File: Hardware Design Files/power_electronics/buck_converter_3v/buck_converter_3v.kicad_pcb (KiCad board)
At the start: 2 copper layers, 34.4 x 28.1 mm, 22 parts, among them J1 Conn_01x02, J2 Conn_01x02

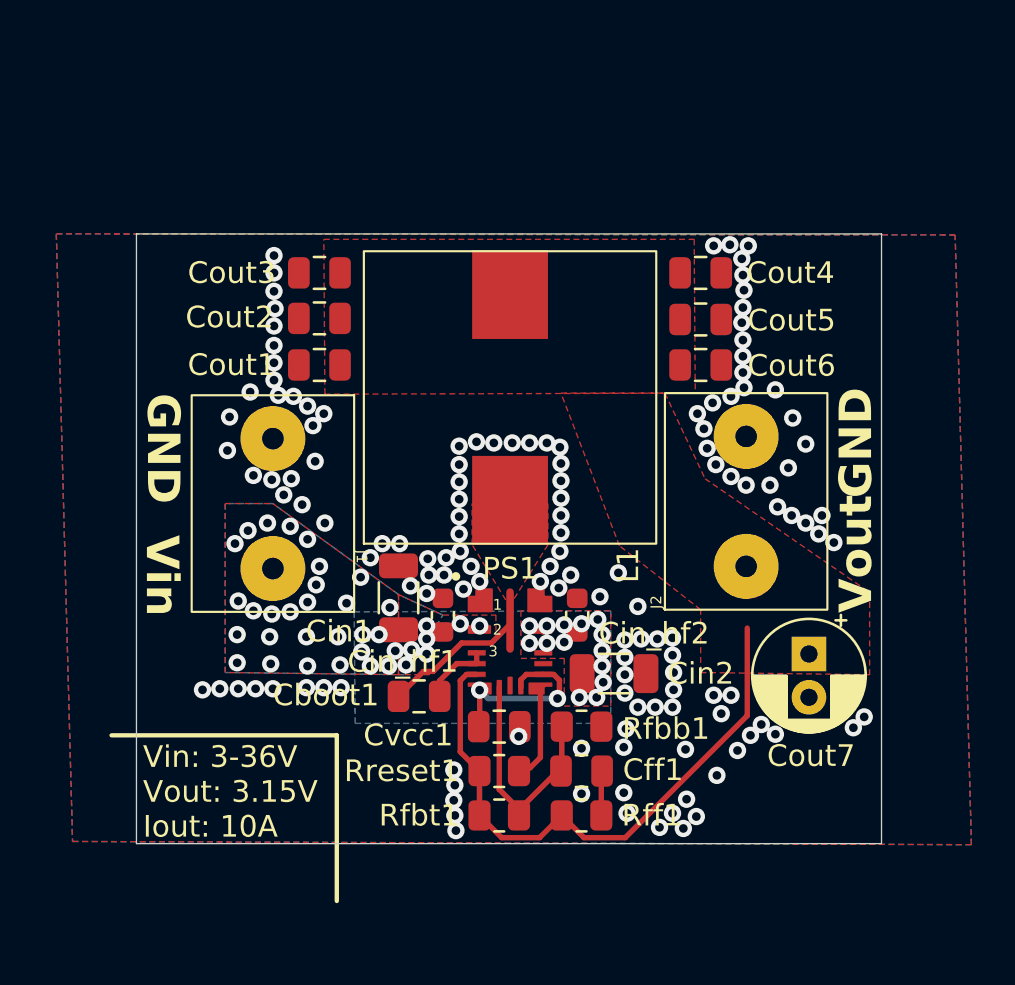
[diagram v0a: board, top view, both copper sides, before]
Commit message: refactor(buck_converter_3v): apply jlcpcb fab design rules
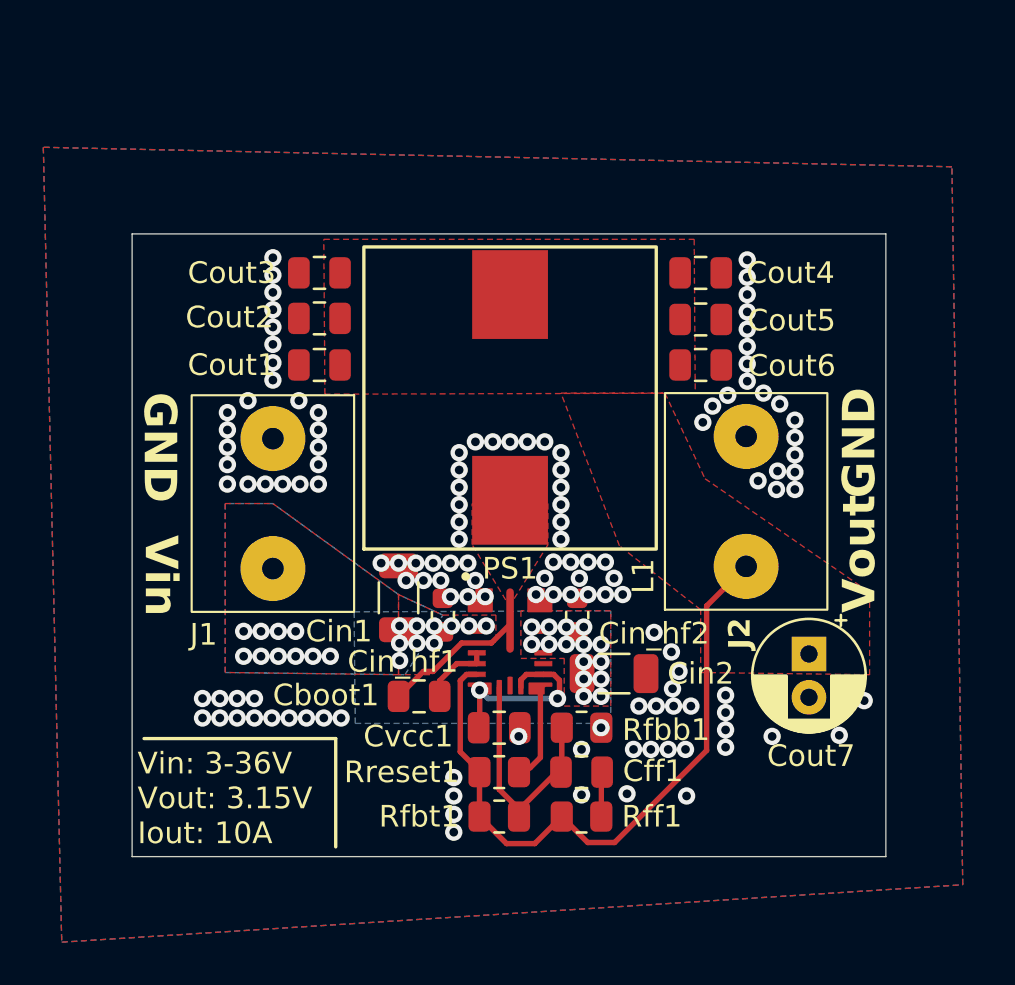
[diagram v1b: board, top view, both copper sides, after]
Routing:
- net /Vout: track 27.5 -> 30.5 mm
- net /Vin: track 0.66 -> 0.00 mm, vias 50 -> 35
- net GND: vias 141 -> 132
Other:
- board size 34.4 x 28.1 mm -> 34.8 x 28.8 mm
- rule pad_to_mask_clearance: 0.0508 -> 0.038

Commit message: feat(buck_converter): unify pcb design, schematic varies by resistor value, add mounting holes
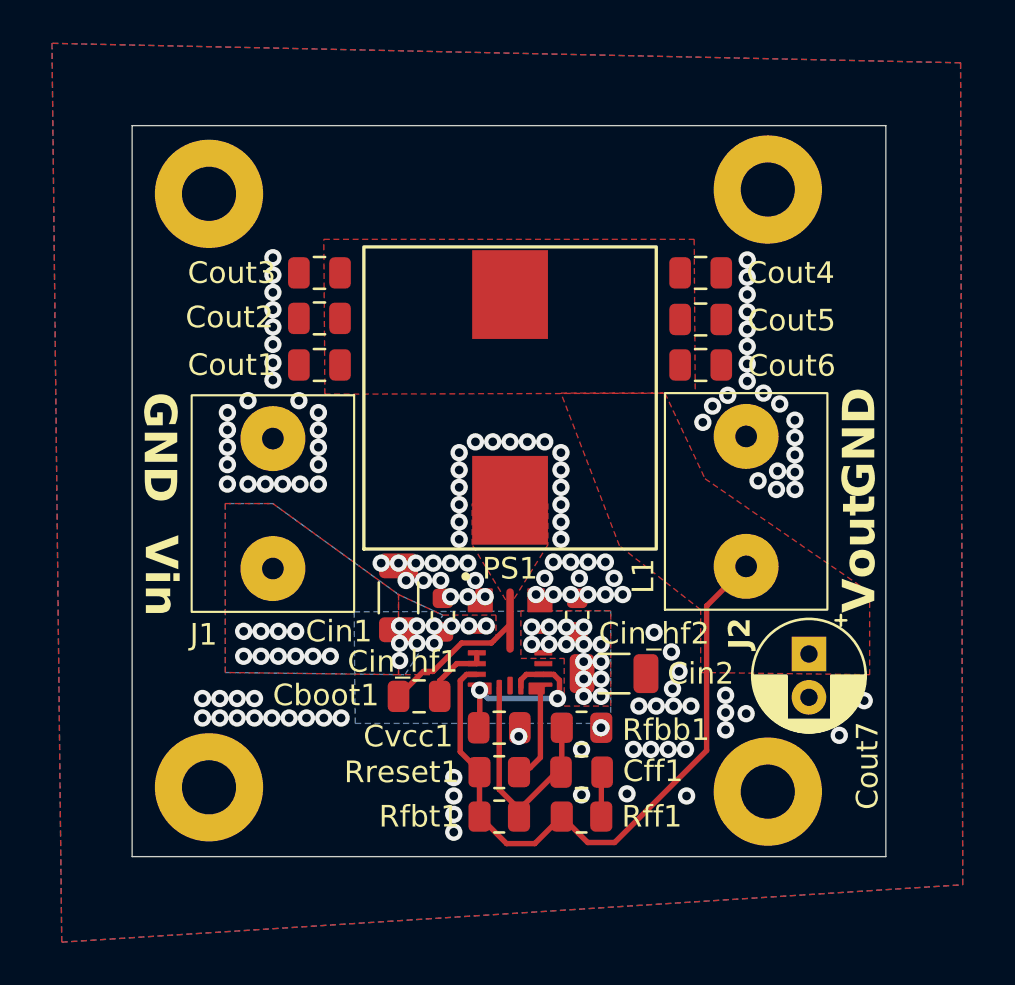
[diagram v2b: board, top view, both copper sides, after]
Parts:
- added H1: MountingHole, MountingHole:MountingHole_2.5mm_Pad, F.Cu at (95.6, 76.2)
- added H2: MountingHole, MountingHole:MountingHole_2.5mm_Pad, F.Cu at (121.4, 76.4)
- added H3: MountingHole, MountingHole:MountingHole_2.5mm_Pad, F.Cu at (121.4, 48.6)
- added H4: MountingHole, MountingHole:MountingHole_2.5mm_Pad, F.Cu at (95.6, 48.8)
- L1: value 2.2u -> 3.3u
- Rfbb1: value 46.5k -> 25.5k
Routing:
- net GND: vias 132 -> 131
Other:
- board size 34.8 x 28.8 mm -> 34.8 x 33.8 mm
- board text removed: "Vin: 3-36V Vout: 3.15V Iout: 10A"
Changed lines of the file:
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@@
     )
   )
+  (footprint "MountingHole:MountingHole_2.5mm_Pad" (layer "F.Cu")
+    (at 121.4 48.6)
+    (descr "Mounting Hole 2.5mm")
+    (tags "mounting hole 2.5mm")
+    (property "Sheetfile" "buck_converter_3v.kicad_sch")
+    (property "Sheetname" "")
+    (property "ki_description" "Mounting Hole without connection")
+    (property "ki_keywords" "mounting hole")
+    (attr exclude_from_pos_files)
+    (fp_text reference "H3" (at 0 -3.5) (layer "F.SilkS") hide
+        (effects (font (size 1 1) (thickness 0.15)))
+    )
+    (fp_text value "MountingHole" (at 0 3.5) (layer "F.Fab")
+        (effects (font (size 1 1) (thickness 0.15)))
+    )
+    (fp_text user "${REFERENCE}" (at 0 0) (layer "F.Fab")
+        (effects (font (size 1 1) (thickness 0.15)))
+    )
+    (fp_circle (center 0 0) (end 2.5 0)
+      (stroke (width 0.15) (type solid)) (fill none) (layer "Cmts.User"))
+    (fp_circle (center 0 0) (end 2.75 0)
+      (stroke (width 0.05) (type solid)) (fill none) (layer "F.CrtYd"))
+    (pad "1" thru_hole circle (at 0 0) (size 5 5) (drill 2.5) (layers "*.Cu" "*.Mask"))
+  )
   (footprint "Resistor_SMD:R_0805_2012Metric" (layer "F.Cu")
     (at 109 75.5)
@@
     (property "ki_keywords" "cap capacitor")
     (attr through_hole)
-    (fp_text reference "Cout7" (at 4.705112 -0.1 180) (layer "F.SilkS")
+    (fp_text reference "Cout7" (at 5.155112 -2.7 -90) (layer "F.SilkS")
         (effects (font (size 1 1) (thickness 0.155)))
     )
@@
     )
   )
+  (footprint "MountingHole:MountingHole_2.5mm_Pad" (layer "F.Cu")
+    (at 95.6 48.8)
+    (descr "Mounting Hole 2.5mm")
+    (tags "mounting hole 2.5mm")
+    (property "Sheetfile" "buck_converter_3v.kicad_sch")
+    (property "Sheetname" "")
+    (property "ki_description" "Mounting Hole without connection")
+    (property "ki_keywords" "mounting hole")
+    (attr exclude_from_pos_files)
+    (fp_text reference "H4" (at 0 -3.5) (layer "F.SilkS") hide
+        (effects (font (size 1 1) (thickness 0.15)))
+    )
+    (fp_text value "MountingHole" (at 0 3.5) (layer "F.Fab")
+        (effects (font (size 1 1) (thickness 0.15)))
+    )
+    (fp_text user "${REFERENCE}" (at 0 0) (layer "F.Fab")
+        (effects (font (size 1 1) (thickness 0.15)))
+    )
+    (fp_circle (center 0 0) (end 2.5 0)
+      (stroke (width 0.15) (type solid)) (fill none) (layer "Cmts.User"))
+    (fp_circle (center 0 0) (end 2.75 0)
+      (stroke (width 0.05) (type solid)) (fill none) (layer "F.CrtYd"))
+    (pad "1" thru_hole circle (at 0 0) (size 5 5) (drill 2.5) (layers "*.Cu" "*.Mask"))
+  )
   (footprint "Capacitor_SMD:C_0805_2012Metric" (layer "F.Cu")
     (at 100.7 56.7 180)
@@
     )
   )
+  (footprint "MountingHole:MountingHole_2.5mm_Pad" (layer "F.Cu")
+    (at 95.6 76.2)
+    (descr "Mounting Hole 2.5mm")
+    (tags "mounting hole 2.5mm")
+    (property "Sheetfile" "buck_converter_3v.kicad_sch")
+    (property "Sheetname" "")
+    (property "ki_description" "Mounting Hole without connection")
+    (property "ki_keywords" "mounting hole")
+    (attr exclude_from_pos_files)
+    (fp_text reference "H1" (at 3.4 2) (layer "F.SilkS") hide
+        (effects (font (size 1 1) (thickness 0.15)))
+    )
+    (fp_text value "MountingHole" (at 0 3.5) (layer "F.Fab")
+        (effects (font (size 1 1) (thickness 0.15)))
+    )
+    (fp_text user "${REFERENCE}" (at 0 0) (layer "F.Fab")
+        (effects (font (size 1 1) (thickness 0.15)))
+    )
+    (fp_circle (center 0 0) (end 2.5 0)
+      (stroke (width 0.15) (type solid)) (fill none) (layer "Cmts.User"))
+    (fp_circle (center 0 0) (end 2.75 0)
+      (stroke (width 0.05) (type solid)) (fill none) (layer "F.CrtYd"))
+    (pad "1" thru_hole circle (at 0 0) (size 5 5) (drill 2.5) (layers "*.Cu" "*.Mask"))
+  )
   (footprint "Capacitor_SMD:C_0603_1608Metric" (layer "F.Cu")
     (at 112.6 68.25 90)
@@
     (descr "Resistor SMD 0805 (2012 Metric), square (rectangular) end terminal, IPC_7351 nominal, (Body size source: IPC-SM-782 page 72, https://www.pcb-3d.com/wordpress/wp-content/uploads/ipc-sm-782a_amendment_1_and_2.pdf), generated with kicad-footprint-generator")
     (tags "resistor")
-    (property "Digikey PN" "ERA-6AEB4642V")
+    (property "Digikey PN" "ERA-6AEB2552V")
     (property "Sheetfile" "buck_converter_3v.kicad_sch")
     (property "Sheetname" "")
@@
         (effects (font (size 1 1) (thickness 0.155)))
     )
-    (fp_text value "46.5k" (at 0 1.65) (layer "F.Fab")
+    (fp_text value "25.5k" (at 0 1.65) (layer "F.Fab")
         (effects (font (size 1 1) (thickness 0.15)))
     )
@@
     )
   )
+  (footprint "MountingHole:MountingHole_2.5mm_Pad" (layer "F.Cu")
+    (at 121.4 76.4)
+    (descr "Mounting Hole 2.5mm")
+    (tags "mounting hole 2.5mm")
+    (property "Sheetfile" "buck_converter_3v.kicad_sch")
+    (property "Sheetname" "")
+    (property "ki_description" "Mounting Hole without connection")
+    (property "ki_keywords" "mounting hole")
+    (attr exclude_from_pos_files)
+    (fp_text reference "H2" (at 3.4 -1) (layer "F.SilkS") hide
+        (effects (font (size 1 1) (thickness 0.15)))
+    )
+    (fp_text value "MountingHole" (at 0 3.5) (layer "F.Fab")
+        (effects (font (size 1 1) (thickness 0.15)))
+    )
+    (fp_text user "${REFERENCE}" (at 0 0) (layer "F.Fab")
+        (effects (font (size 1 1) (thickness 0.15)))
+    )
+    (fp_circle (center 0 0) (end 2.5 0)
+      (stroke (width 0.15) (type solid)) (fill none) (layer "Cmts.User"))
+    (fp_circle (center 0 0) (end 2.75 0)
+      (stroke (width 0.05) (type solid)) (fill none) (layer "F.CrtYd"))
+    (pad "1" thru_hole circle (at 0 0) (size 5 5) (drill 2.5) (layers "*.Cu" "*.Mask"))
+  )
   (footprint "custom_footprints:TMPC 1004H-3R3MG-D" (layer "F.Cu")
     (at 109.5 58.2 90)
@@
         (effects (font (size 1 1) (thickness 0.155)))
     )
-    (fp_text value "2.2u" (at 0 7.9 90 unlocked) (layer "F.Fab")
+    (fp_text value "3.3u" (at 0 7.9 90 unlocked) (layer "F.Fab")
         (effects (font (size 1 1) (thickness 0.15)))
     )
@@
     )
   )
-  (gr_line (start 101.45 73.95) (end 101.45 78.95)
-    (stroke (width 0.155) (type default)) (layer "F.SilkS"))
-  (gr_line (start 92.6 73.95) (end 101.45 73.95)
-    (stroke (width 0.155) (type default)) (layer "F.SilkS"))
-  (gr_rect (start 92.05 50.65) (end 126.85 79.4)
+  (gr_rect (start 92.05 45.65) (end 126.85 79.4)
     (stroke (width 0.01) (type default)) (fill none) (layer "Edge.Cuts"))
   (gr_text "Vout" (at 126.5 68.15 90) (layer "F.SilkS")
@@
     (effects (font (size 1.5 1.5) (thickness 0.3) bold) (justify left bottom))
   )
-  (gr_text "Vin: 3-36V\nVout: 3.15V\nIout: 10A" (at 92.3 78.9) (layer "F.SilkS")
-    (effects (font (size 1 1) (thickness 0.155)) (justify left bottom))
-  )
-  (dimension (type aligned) (layer "User.1")
-    (pts (xy 92.25 50.65) (xy 126.65 50.65))
-    (height -10)
-    (gr_text "34.4000 mm" (at 109.45 39.5) (layer "User.1")
+  (dimension (type aligned) (layer "Cmts.User")
+    (pts (xy 126.85 45.65) (xy 92.05 45.65))
+    (height 11.849999)
+    (gr_text "34.8000 mm" (at 109.45 32.650001) (layer "Cmts.User")
       (effects (font (size 1 1) (thickness 0.15)))
     )
@@
     (style (thickness 0.15) (arrow_length 1.27) (text_position_mode 0) (extension_height 0.58642) (extension_offset 0.5) keep_text_aligned)
   )
-  (dimension (type aligned) (layer "User.1")
-    (pts (xy 126.65 50.65) (xy 126.65 78.8))
-    (height -15.15)
-    (gr_text "28.1500 mm" (at 140.65 64.725 90) (layer "User.1")
+  (dimension (type aligned) (layer "Cmts.User")
+    (pts (xy 126.85 45.65) (xy 126.85 79.4))
+    (height -9.75)
+    (gr_text "33.7500 mm" (at 135.45 62.525 90) (layer "Cmts.User")
       (effects (font (size 1 1) (thickness 0.15)))
     )
@@
   (segment (start 111.8875 73.25) (end 111.8875 75.2625) (width 0.25) (layer "F.Cu") (net 3))
   (via (at 116.15 69.05) (size 0.8) (drill 0.4) (layers "F.Cu" "B.Cu") (free) (net 4))
-  (via (at 119.45 74.35) (size 0.8) (drill 0.4) (layers "F.Cu" "B.Cu") (free) (net 4))
   (via (at 122.65 60.05) (size 0.8) (drill 0.4) (layers "F.Cu" "B.Cu") (free) (net 4))
   (via (at 125.85 72.2) (size 0.8) (drill 0.4) (layers "F.Cu" "B.Cu") (free) (net 4))
@@
   (via (at 111.5 67.299998) (size 0.8) (drill 0.4) (layers "F.Cu" "B.Cu") (free) (net 4))
   (via (at 113.1 67.299998) (size 0.8) (drill 0.4) (layers "F.Cu" "B.Cu") (free) (net 4))
-  (via (at 121.6 73.85) (size 0.8) (drill 0.4) (layers "F.Cu" "B.Cu") (free) (net 4))
+  (via (at 120.4 72.8) (size 0.8) (drill 0.4) (layers "F.Cu" "B.Cu") (free) (net 4))
   (via (at 121.95 58.5) (size 0.8) (drill 0.4) (layers "F.Cu" "B.Cu") (free) (net 4))
   (via (at 120.449998 55.85) (size 0.8) (drill 0.4) (layers "F.Cu" "B.Cu") (free) (net 4))
@@
     (polygon
       (pts
-        (xy 129.9 47.55)
-        (xy 87.95 46.65)
+        (xy 130.3 42.75)
+        (xy 88.35 41.85)
         (xy 88.8 83.35)
         (xy 130.4 80.7)
